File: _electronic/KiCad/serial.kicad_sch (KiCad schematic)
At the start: 16 parts

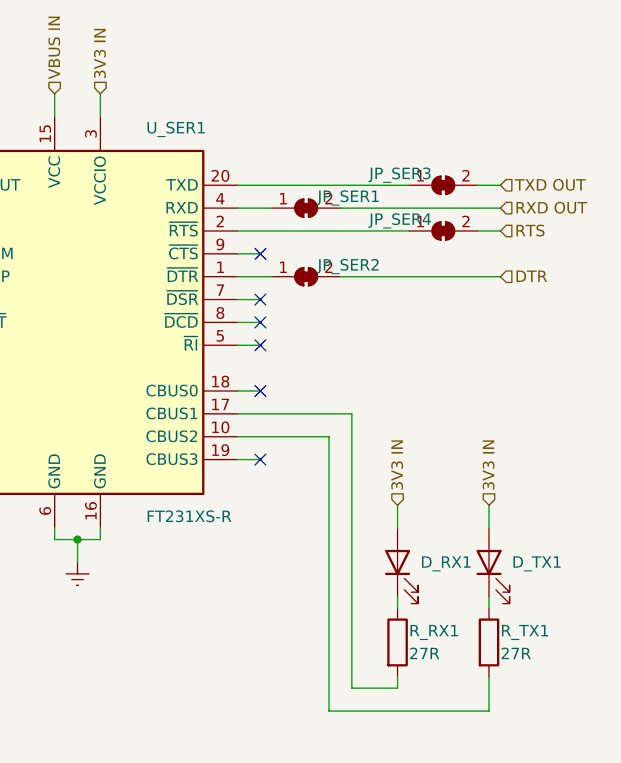
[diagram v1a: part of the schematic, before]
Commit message: external flashing header
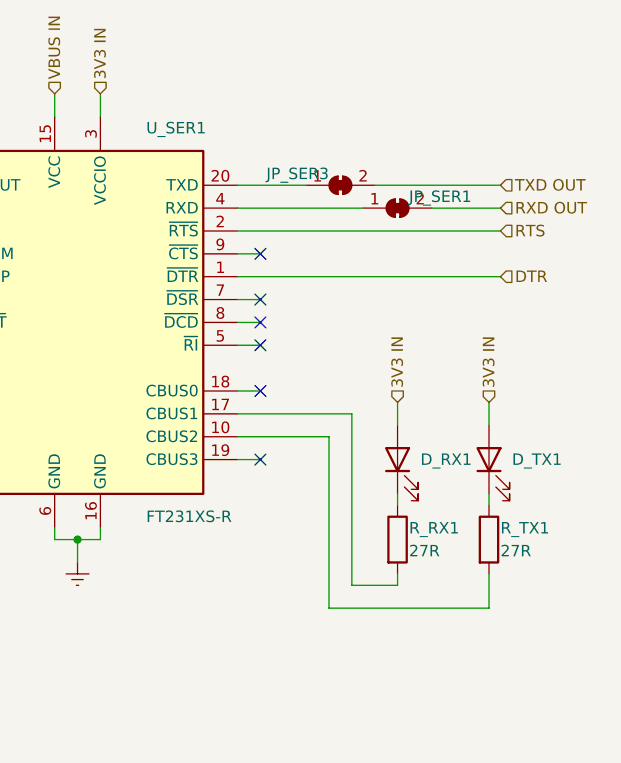
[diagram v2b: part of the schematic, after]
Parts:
- removed JP_SER2, JP_SER4: Bridged, Jumper:SolderJumper-2_P1.3mm_Bridged2Bar_Pad1.0x1.5mm, symbol Jumper:SolderJumper_2_Bridged
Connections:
- net DTR: now also U_SER1.1 (~{DTR})
- net RTS: now also U_SER1.2 (~{RTS})
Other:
- moved on the sheet: D_RX1, D_TX1, JP_SER1, JP_SER3, R_RX1, R_TX1

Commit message: schematics footer and export
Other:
- company: (none) -> Andrei Speridiao
- title: (none) -> E-TKT
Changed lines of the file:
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@@
 (kicad_sch (version 20211123) (generator eeschema)
   (paper "A4")
+  (title_block
+    (title "E-TKT")
+    (date "2022-07-21")
+    (rev "3")
+    (company "Andrei Speridiao")
+  )
   (junction (at 130.81 77.47) (diameter 0) (color 0 0 0 0)
   )
